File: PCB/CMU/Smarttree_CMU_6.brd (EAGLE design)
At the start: 88.4 x 55 mm, 77 parts

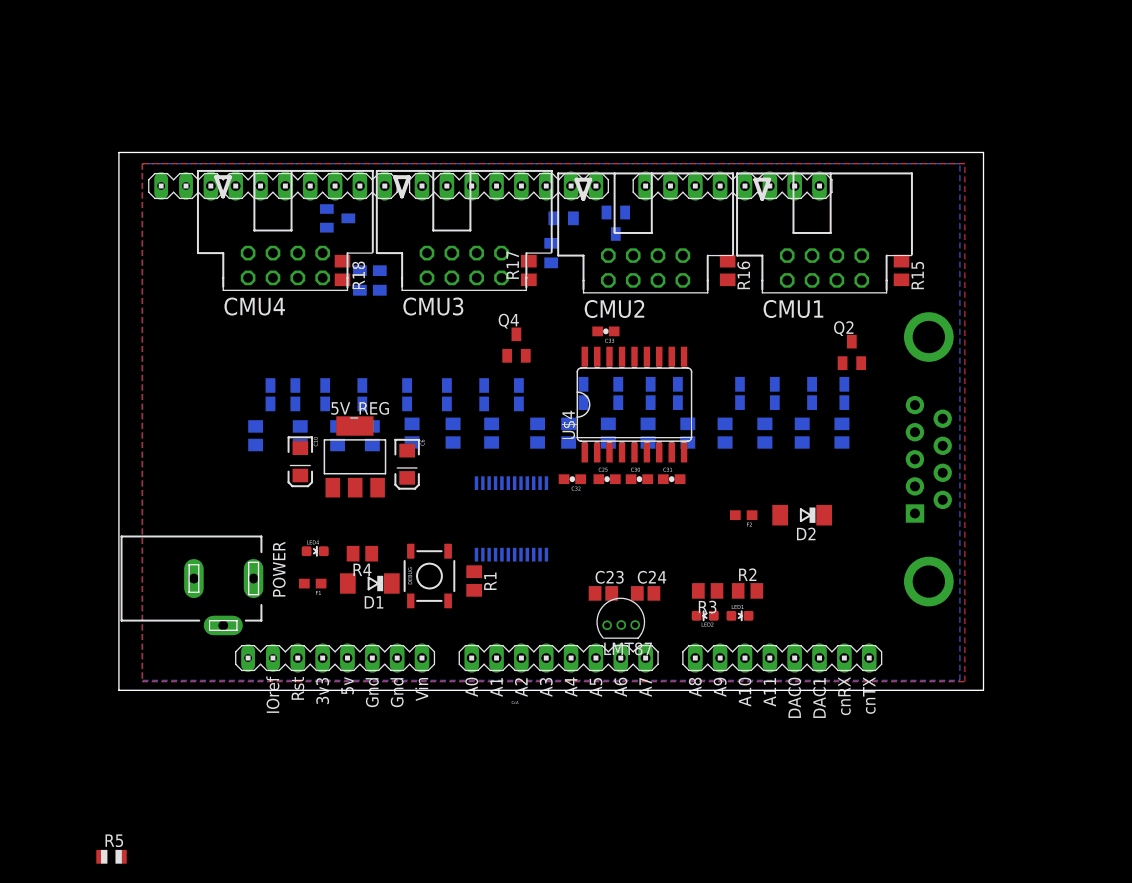
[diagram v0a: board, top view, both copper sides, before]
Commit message: BMS with the new connectors
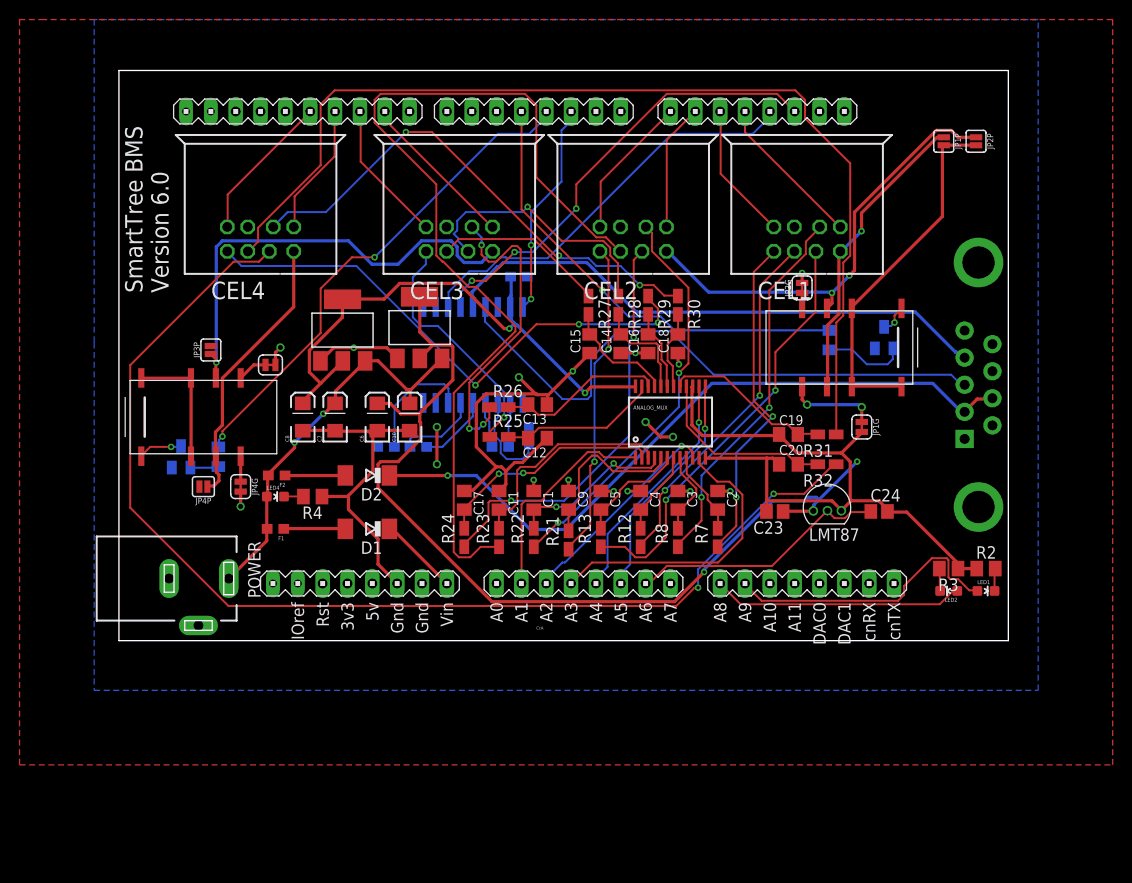
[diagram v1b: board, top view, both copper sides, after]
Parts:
- removed CMU1, CMU2, CMU3, CMU4: 057-006-0, con-panduit:057-006-0
- removed DEBUG: (no value), SparkFun-Electromechanical:TACTILE_SWITCH_SMD
- removed Q2, Q3, Q5: (no value), adafruit:SOT23
- removed R1: 330, adafruit:M0805
- removed R10, R11, R14: 330, adafruit:R0805
- removed R15, R16, R17, R18: bypass, adafruit:M0805
- added 3V3_REG: REG1117, burr-brown:SOT223
- added C7: 0.1uF, SparkFun-Retired:EIA3216
- added C8: 10uF, SparkFun-Retired:EIA3216
- added CEL1, CEL2, CEL3, CEL4: 8PINCONN, SmartTreeCan:8PINCONN
- added JP1G, JP2G, JP3G, JP4G: JUMPER-SMT_2_NC_TRACE_SILK, SparkFun-Jumpers:SMT-JUMPER_2_NC_TRACE_SILK
- added JP1P, JP2P, JP3P, JP4P: JUMPER-SMT_2_NO_SILK, SparkFun-Jumpers:SMT-JUMPER_2_NO_SILK
- added Q1: (no value), adafruit:SOT23
- added U$2, U$3: RELAY-SINGLE_LATCH, SmartTreeCan:RELAY-EE2
- R5: value 1M -> 330
- moved R31 51.5 mm to (72.4, 26.2), flipped to the top, turned to 180 degrees
- moved R32 48.0 mm to (72.4, 23.1), flipped to the top, turned to 180 degrees
- moved F2 47.9 mm to (16.1, 22.0)
- moved C19 46.1 mm to (68.5, 26.2), flipped to the top, turned to 0 degrees
- moved D2 44.6 mm to (25.4, 22.0)
- moved C20 42.6 mm to (68.5, 23.1), flipped to the top, turned to 0 degrees
- moved R5 42.3 mm to (10.2, 23.9), flipped to the bottom, turned to 90 degrees
- moved C16 41.2 mm to (54.1, 35.4), flipped to the top
- moved R30 40.2 mm to (57.1, 39.4), flipped to the top
- moved C18 39.7 mm to (57.1, 35.4), flipped to the top
- moved R29 39.7 mm to (54.1, 39.4), flipped to the top
- moved Q4 37.6 mm to (78.2, 36.1), flipped to the bottom
- moved R9 29.8 mm to (72.6, 35.8)
- moved C31 29.4 mm to (27.3, 24.9), flipped to the bottom
- moved R24 26.3 mm to (35.3, 15.6), flipped to the top, turned to 90 degrees
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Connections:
- net !RES_CEL1 renamed !RES_CEL_1&2
- net N$4 renamed SCRN_PWR
- removed net !RES_CEL2: R10.2, U$1.3
- removed net !RES_CEL3: R11.2, U$1.5
- removed net !RES_CEL4: R14.2, U$1.6
- removed net CEL1_GND: CMU1.1, Q2.3, R15.2, R5.2
- removed net CEL2_GND: CMU2.1, Q3.3, R16.2
- removed net CEL3_GND: CMU3.1, Q4.3, R17.2
- removed net CEL4_GND: CMU4.1, Q5.3, R18.2
- new net !RES_CEL_3&4: R5.2, U$1.3
- new net N$1: JP1G.1, U$2.P$5
- new net N$10: JP3G.1, U$3.P$5
- new net N$11: JP4G.1, U$3.P$8
- new net N$21: JP2G.1, U$2.P$8
- net 12V: now also 3V3_REG.3, C7.A
- net 3.3V: now also 3V3_REG.2, 3V3_REG.4, C8.A; no longer R1.2, U$1.3V3
- net 5V: now also 5V_REG.4, JP1P.2, JP2P.2, JP3P.2, JP4P.2, U$2.P$1, U$2.P$10, U$2.P$3, U$3.P$1, U$3.P$10, U$3.P$3; no longer R5.1
- net BUTTON: no longer DEBUG.3, DEBUG.4, R1.1
- net CEL1_PWR: now also CEL1.8, JP1P.1, U$2.P$4; no longer CMU1.7
- net CEL2_PWR: now also CEL2.8, JP2P.1, U$2.P$9; no longer CMU2.7
- net CEL3_PWR: now also CEL3.8, JP3P.1, U$3.P$4; no longer CMU3.7
- net CEL4_PWR: now also CEL4.8, JP4P.1, U$3.P$9; no longer CMU4.7
- net CSI1: now also CEL1.4; no longer CMU1.4
- net CSI2: now also CEL2.4; no longer CMU2.4
- net CSI3: now also CEL3.4; no longer CMU3.4
- net CSI4: now also CEL4.4; no longer CMU4.4
- net CSO1: now also CEL1.2; no longer CMU1.2
- net CSO2: now also CEL2.2; no longer CMU2.2
- net CSO3: now also CEL3.2; no longer CMU3.2
- net CSO4: now also CEL4.2; no longer CMU4.2
- net GND: now also 3V3_REG.1, C7.C, C8.C, CEL1.1, CEL2.1, CEL3.1, CEL4.1, JP1G.2, JP2G.2, JP3G.2, JP4G.2, Q1.2; no longer DEBUG.1, DEBUG.2, Q2.2, Q3.2, Q5.2, R15.1, R16.1, R17.1, R18.1
- net N$3: now also Q4.3, U$2.P$12; no longer Q3.1, R10.1
- net N$6: now also Q4.1; no longer Q2.1
- net N$7: now also Q1.1, R5.1; no longer Q4.1, R11.1
- net N$9: now also Q1.3, U$3.P$12; no longer Q5.1, R14.1
- net RI1: now also CEL1.3; no longer CMU1.3
- net RI2: now also CEL2.3; no longer CMU2.3
- net RI3: now also CEL3.3; no longer CMU3.3
- net RI4: now also CEL4.3; no longer CMU4.3
- net RO1: now also CEL1.5; no longer CMU1.5
- net RO2: now also CEL2.5; no longer CMU2.5
- net RO3: now also CEL3.5; no longer CMU3.5
- net RO4: now also CEL4.5; no longer CMU4.5
- net RX: now also X2.2; no longer X2.3
- net TS1: now also CEL1.6; no longer CMU1.6
- net TS2: now also CEL2.6; no longer CMU2.6
- net TS3: now also CEL3.6; no longer CMU3.6
- net TS4: now also CEL4.6; no longer CMU4.6
- net TX: now also X2.3; no longer X2.2
- net VS1: now also CEL1.7; no longer CMU1.8
- net VS2: now also CEL2.7; no longer CMU2.8
- net VS3: now also CEL3.7; no longer CMU3.8
- net VS4: now also CEL4.7; no longer CMU4.8
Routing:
- net GND: track 0.00 -> 170.8 mm, vias 0 -> 18
- net 5V: track 0.00 -> 147.9 mm, vias 0 -> 2
- net VS4: track 0.00 -> 117.0 mm, vias 0 -> 2
- net CSI4: track 0.00 -> 105.4 mm
- net CSI2: track 0.00 -> 97.0 mm
- net SCRN_PWR: track 0.00 -> 71.9 mm, vias 0 -> 1
- net TX: track 0.00 -> 61.2 mm
- net 3.3V: track 0.00 -> 57.5 mm, vias 0 -> 2
- net RX: track 0.00 -> 57.2 mm
- net TS4: track 0.00 -> 55.5 mm, vias 0 -> 3
- net CSO4: track 0.00 -> 52.4 mm, vias 0 -> 3
- net !RES_CEL_3&4: track 0.00 -> 51.4 mm, vias 0 -> 2
- net CEL3_PWR: track 0.00 -> 46.9 mm, vias 0 -> 1
- net !RES_CEL_1&2: track 0.00 -> 46.6 mm, vias 0 -> 1
- net RX1: track 0.00 -> 46.3 mm, vias 0 -> 3
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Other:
- board size 88.4 x 55 mm -> 90.9 x 58.3 mm
- board text added: "----Layout ->make it nicer ->put analog MUX on the top layer ->make a debugging interface for sensor reading ->switch bypass with jumper -> DONE make sensor board connectors closer to the edge -> add back 5V top and GND bottom planes"
- board text added: "SmartTree BMS Version 6.0"
- board text removed: "----Layout ->make it nicer ->put analog MUX on the top layer ->make a debugging interface for sensor reading ->switch bypass with jumper ->make sensor board connectors closer to the edge"
